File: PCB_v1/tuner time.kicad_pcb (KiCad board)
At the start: 4 copper layers, 80 x 40 mm, 109 parts, among them J1 B6B-PH-K-S, J10 1051640001, J2 B6B-PH-K-S, J3 S2B-PH-K-SLFSN, J4 Conn_01x05_Pin, J5 Conn_01x05_Pin, J6 Conn_02x04_Odd_Even, J7 B4B-XH-A, J8 Conn_ARM_JTAG_SWD_10, J9 Conn_01x03, SW1 SW_SPST, SW2 SW_Push, SW3 SW_Push, SW4 SW_Push, SW5 SW_Push, SW6 SW_Push, SW7 SW_Push, SW8 SW_Push, SW9 SW_SPDT, U1 C1F 2, U2 BQ25185DLHR, U3 BQ27441-G1, U4 DRV8834PWP, U5 STM32F405RGTx, U6 ESD9B5.0ST5G, Y1 ASE-8MHz-L-C-T

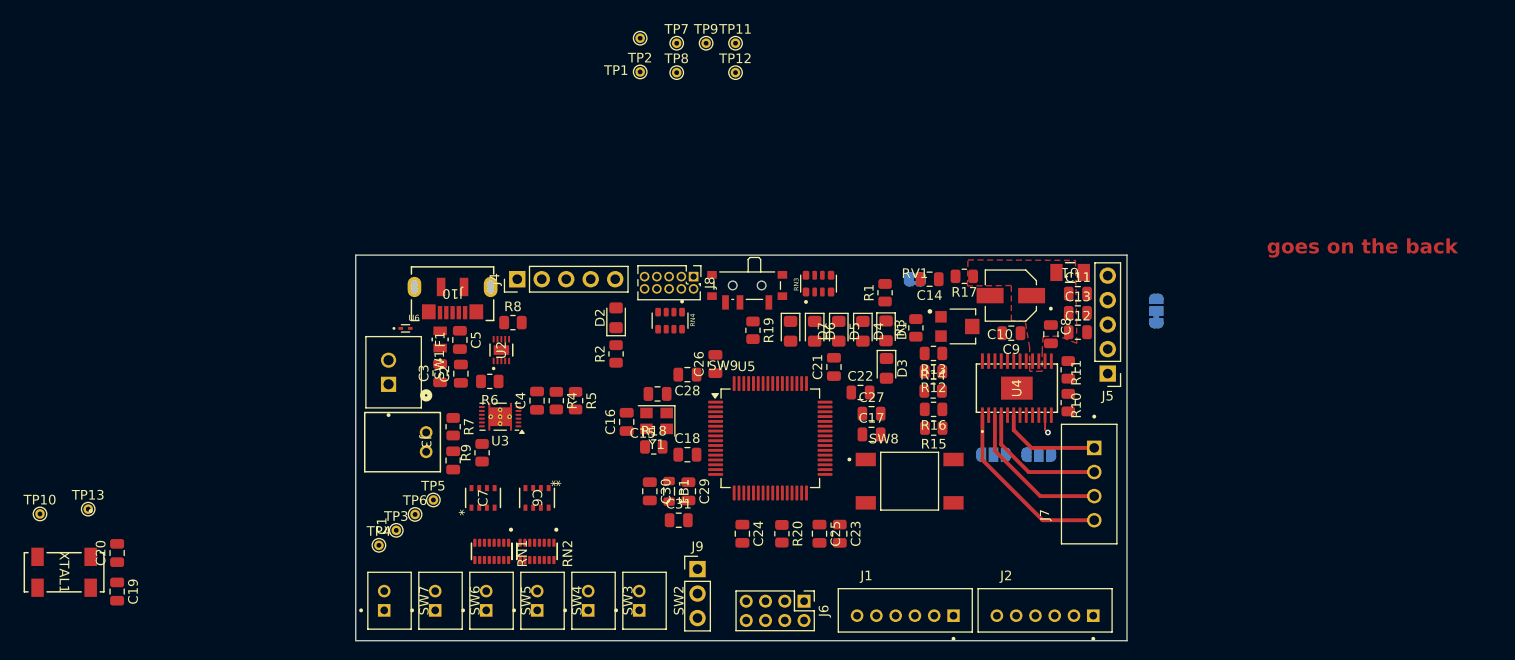
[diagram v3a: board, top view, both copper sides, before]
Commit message: Main routes done, no power planes, no DRC
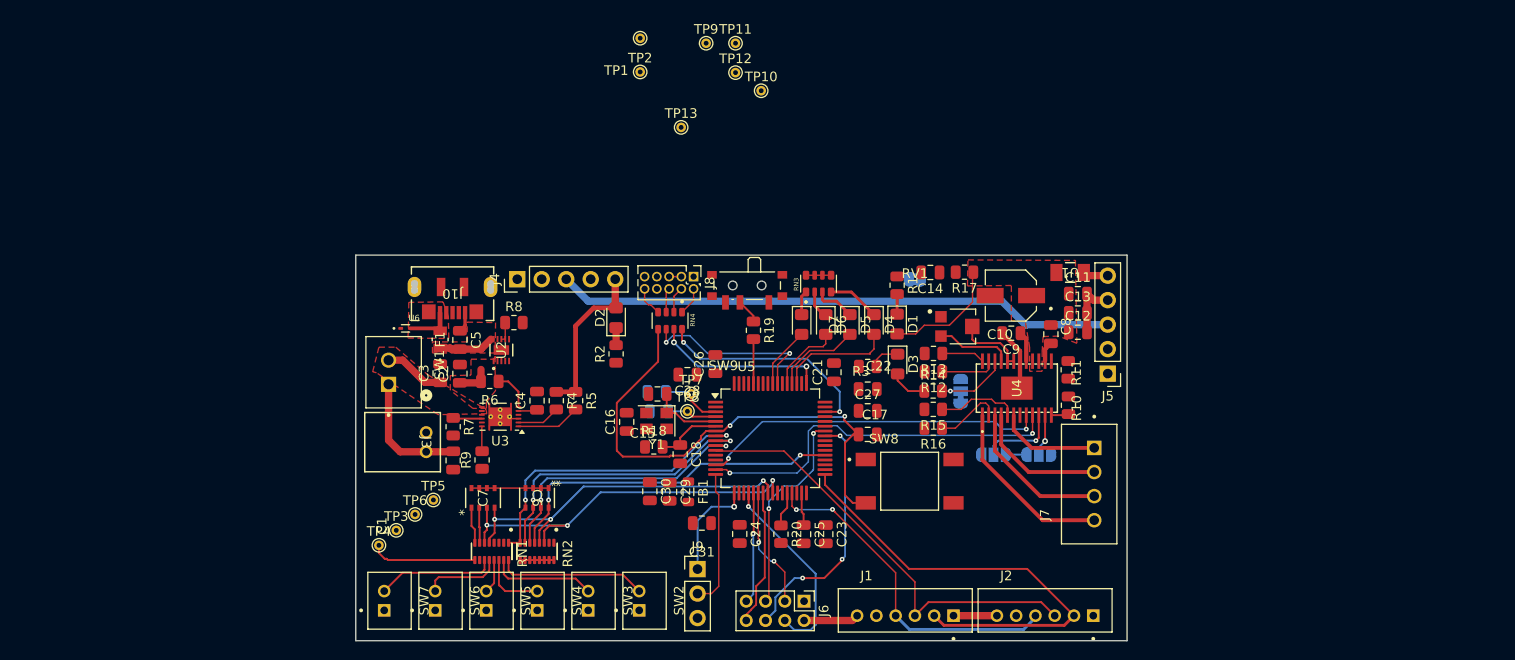
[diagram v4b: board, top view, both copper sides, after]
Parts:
- removed XTAL1: MC-306 32.7680K-E3:ROHS, Parts_Library:SO4_MC-306_SEC
- C19, C20: moved to B.Cu
- moved TP10 86.7 mm to (192.1, 83.0)
- moved TP13 73.2 mm to (183.8, 86.8)
- moved C19 59.7 mm to (181.2, 114.2), turned to 180 degrees
- moved C20 58.1 mm to (181.4, 116.2), turned to 180 degrees
- moved TP7 36.4 mm to (184.8, 114.4)
- moved TP8 35.1 mm to (184.4, 116.2)
- moved JP4 21.9 mm to (212.8, 114.1)
- moved R3 6.40 mm to (203.1, 111.5), turned to 180 degrees
- moved C31 2.42 mm to (185.9, 127.8), turned to 180 degrees
- moved FB1 2.00 mm to (184.5, 124.5)
- moved R15 1.95 mm to (209.9, 116.0)
- moved C29 1.95 mm to (182.6, 124.5)
- moved R16 1.95 mm to (209.9, 118.0)
- moved C25 1.65 mm to (196.4, 128.9)
- moved R1 1.47 mm to (206.2, 103.1), turned to -90 degrees
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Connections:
- D1 pad 2: 5V -> VMOT
- R3 pad 2: AGND -> GND
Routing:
- net VSYS: track 0.00 -> 61.7 mm
- net NRST: track 0.00 -> 52.5 mm, vias 0 -> 2
- net I2S_WS: track 0.00 -> 47.9 mm
- net I2S_DATA: track 0.00 -> 45.5 mm
- net Button6: track 0.00 -> 40.7 mm, vias 0 -> 3
- net DIR: track 0.00 -> 39.3 mm, vias 0 -> 2
- net Button5: track 0.00 -> 37.8 mm, vias 0 -> 3
- net Button4: track 0.00 -> 36.5 mm, vias 0 -> 2
- net STEP: track 0.00 -> 36.1 mm, vias 0 -> 2
- net 3V3: track 0.00 -> 35.8 mm
- net I2S_BCLK: track 0.00 -> 35.3 mm, vias 0 -> 2
- net Button1: track 0.00 -> 31.9 mm, vias 0 -> 2
- net Button2: track 0.00 -> 30.5 mm, vias 0 -> 2
- net Button3: track 0.00 -> 28.5 mm, vias 0 -> 2
- net DC: track 0.00 -> 26.2 mm, vias 0 -> 3
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- added copper zone on F.Cu, net BATT_POS
- added copper zone on F.Cu, net Net-(J10-VBUS)
- added copper zone on F.Cu, net VBUS
- added copper zone on F.Cu, net VSYS
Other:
- board text removed: "goes on the back"

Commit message: Power Layout done
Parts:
- added D8: Red, LED_SMD:LED_0805_2012Metric_Pad1.15x1.40mm_HandSolder, F.Cu at (172.1, 108.2)
- added D9: Red, LED_SMD:LED_0805_2012Metric_Pad1.15x1.40mm_HandSolder, F.Cu at (174.6, 108.1)
- added H1: MountingHole, MountingHole:MountingHole_2.2mm_M2_DIN965_Pad_TopOnly, F.Cu at (152.7, 102.7)
- added H2: MountingHole, MountingHole:MountingHole_2.2mm_M2_DIN965_Pad_TopOnly, F.Cu at (235.7, 139.8)
- added R21: 680, Resistor_SMD:R_0805_2012Metric, F.Cu at (172.1, 111.8)
- added R22: 1k, Resistor_SMD:R_0805_2012Metric, F.Cu at (174.6, 111.8)
- added R23: 10k, Resistor_SMD:R_0805_2012Metric, F.Cu at (164.5, 109.9)
- added U7: SMS05T1G, Parts_Library:SOIC_05T1G_ONS, F.Cu at (174.8, 130.6)
- added U8: SMS05T1G, Parts_Library:SOIC_05T1G_ONS, F.Cu at (159.8, 130.5)
- added XTAL1: MC-306 32.7680K-E3:ROHS, Parts_Library:SO4_MC-306_SEC, B.Cu at (168.3, 89.4)
- C2: value 10uF -> 22uF
- C3, C5: value 1uF -> 22uF
- J3: value S2B-PH-K-SLFSN -> JST_B2B-XH-A; footprint Parts_Library:CONN_S2B-PH-K-S_JST -> Parts_Library:JST_B2B-XH-A
- moved JP3 29.2 mm to (244.0, 129.5)
- moved JP2 19.3 mm to (238.8, 128.0)
- moved J3 11.0 mm to (153.7, 128.8)
- moved U2 10.2 mm to (155.0, 111.5)
- moved R6 9.53 mm to (154.6, 115.3), turned to 90 degrees
- moved R15 9.52 mm to (217.6, 121.6), turned to -90 degrees
- moved C1 9.47 mm to (163.8, 112.6), turned to -90 degrees
- moved C5 9.23 mm to (151.6, 109.8), turned to 90 degrees
- moved C2 9.21 mm to (151.6, 113.1)
- moved SW1 8.83 mm to (153.7, 121.0)
- moved R9 8.62 mm to (170.5, 116.8)
- moved TP3 7.65 mm to (160.7, 124.5)
- moved TP4 7.53 mm to (147.2, 135.6)
- moved R16 6.81 mm to (215.7, 121.6), turned to -90 degrees
- moved U6 4.81 mm to (159.9, 108.1), turned to 180 degrees
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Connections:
- net Net-(RN1A-R1.2) renamed /UI/B1
- net Net-(RN1B-R2.2) renamed /UI/B2
- net Net-(RN1C-R3.2) renamed /UI/B3
- net Net-(RN1D-R4.2) renamed /UI/B4
- net Net-(RN1E-R5.2) renamed /UI/B5
- net Net-(RN1F-R6.2) renamed /UI/B6
- net Net-(RN1G-R7.1) renamed /UI/B7
- net Net-(RN1H-R8.1) renamed /UI/B8
- C1 pad 2: Net-(SW1-A) -> BATT_POS
- C16 pad 1: +3.3V -> 3V3
- C21 pad 1: +3.3V -> 3V3
- C22 pad 1: +3.3V -> 3V3
- C23 pad 1: +3.3V -> 3V3
- C24 pad 1: +3.3V -> 3V3
- C26 pad 1: +3.3V -> 3V3
- C28 pad 1: +3.3V -> 3V3
- C3 pad 1: BATT_POS -> VBAT
- C31 pad 1: +3.3V -> 3V3
- FB1 pad 2: +3.3V -> 3V3
- J8 pad 1: +3.3V -> 3V3
- R6 pad 2: VSYS -> VBAT
- R9 pad 2: Net-(U3-GPOUT) -> BAT_EMPTY
- SW9 pad 1: +3V3 -> 3V3
- U2 pad 2: BATT_POS -> VBAT
- U2 pad 3: unconnected-(U2-STAT2-Pad3) -> STATS2
- U2 pad 6: GND -> Net-(U2-TS/MR)
- U2 pad 9: unconnected-(U2-STAT1-Pad9) -> STATS1
- U3 pad 12: Net-(U3-GPOUT) -> BAT_EMPTY
- U3 pad 7: VSYS -> VBAT
- U5 pad 1: +3.3V -> 3V3
- U5 pad 19: +3.3V -> 3V3
- U5 pad 32: +3.3V -> 3V3
- U5 pad 43: unconnected-(U5-PA10-Pad43) -> BAT_EMPTY
- U5 pad 48: +3.3V -> 3V3
- U5 pad 64: +3.3V -> 3V3
- Y1 pad 4: +3.3V -> 3V3
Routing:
- net DIR: track 39.3 -> 0.00 mm, vias 2 -> 0
- net NRST: track 52.5 -> 27.7 mm, vias 2 -> 3
- net Button6: track 40.7 -> 19.8 mm, vias 3 -> 1
- net BATT_POS: track 10.4 -> 28.1 mm
- net Button2: track 30.5 -> 13.0 mm
- net Button1: track 31.9 -> 14.6 mm
- net Button4: track 36.5 -> 19.5 mm
- net Button3: track 28.5 -> 11.5 mm
- net Button5: track 37.8 -> 20.8 mm, vias 3 -> 1
- net /Motor/A1: track 18.8 -> 2.10 mm
- net 3V3: track 35.8 -> 19.9 mm
- net /Motor/A2: track 15.9 -> 1.76 mm
- net Net-(SW1-A): track 13.0 -> 0.00 mm
- net Net-(RN1H-R8.2): track 11.1 -> 0.00 mm
- net /Motor/B1: track 10.7 -> 0.00 mm
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- added copper zone on F.Cu, net GND
- added copper zone on F.Cu, net VBAT

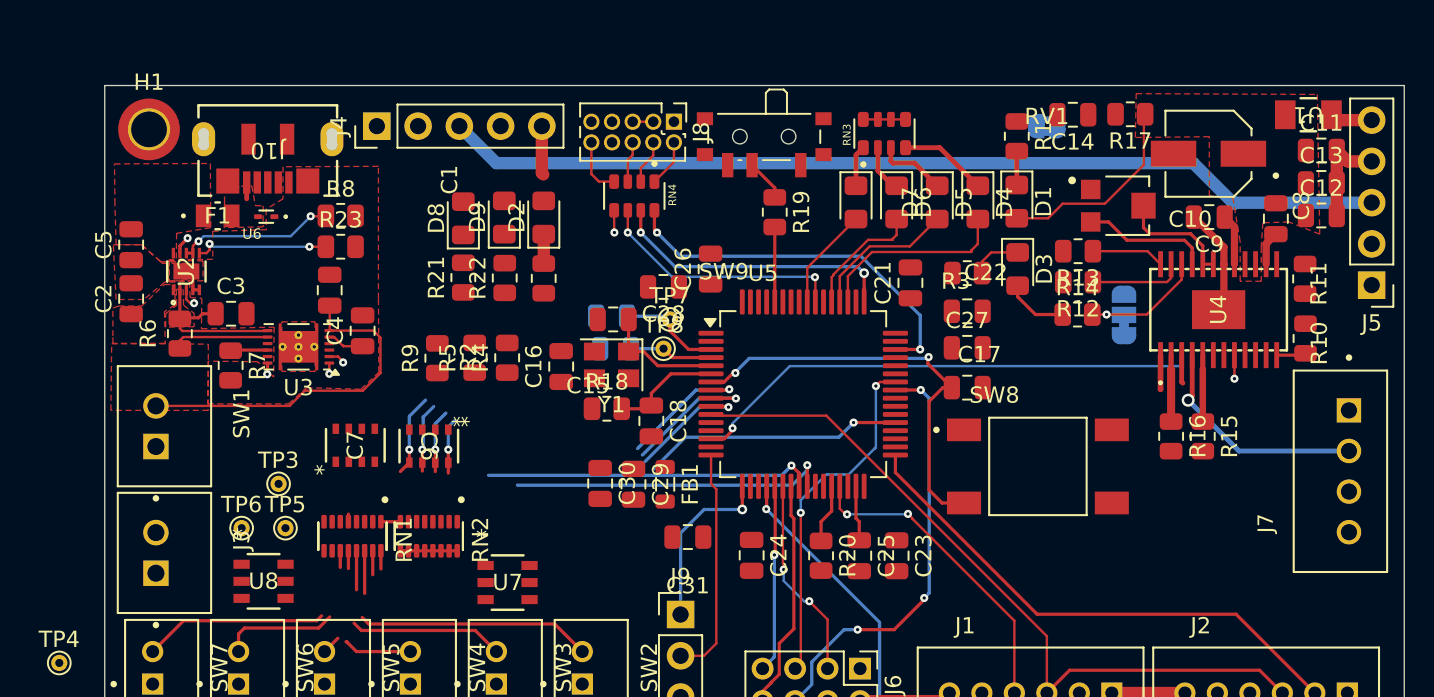
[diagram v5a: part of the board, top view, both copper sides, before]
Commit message: adding the libraries and the new bom for footprint
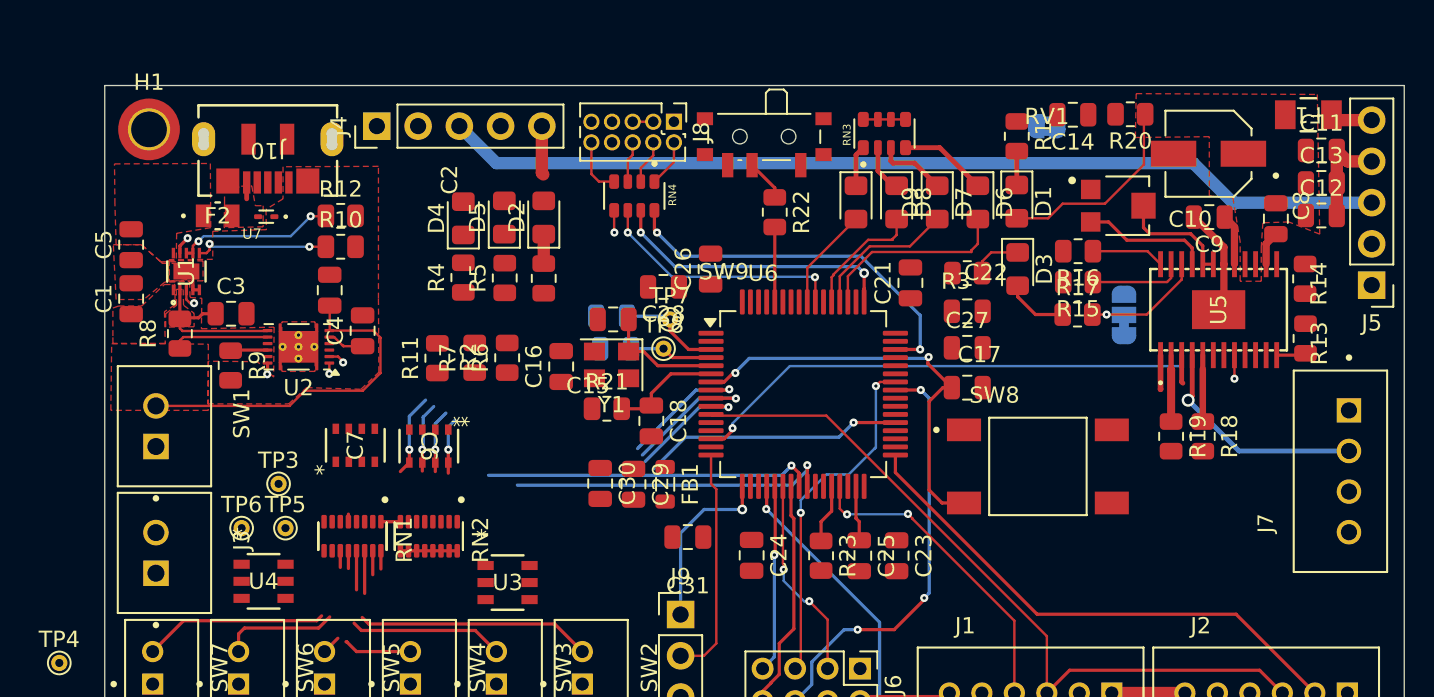
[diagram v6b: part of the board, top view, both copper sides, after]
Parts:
- renumbered C2 to C1, C1 to C2, D8 to D4, D9 to D5, D4 to D6, D5 to D7, D6 to D8, D7 to D9, U1 to F1, F1 to F2, R23 to R10, R9 to R11, R8 to R12, R10 to R13, R11 to R14, R12 to R15, R13 to R16, R14 to R17, R15 to R18, R16 to R19, R17 to R20, R18 to R21, R19 to R22, R20 to R23, R21 to R4, R22 to R5, R4 to R6, R5 to R7, R6 to R8, R7 to R9, U2 to U1, U3 to U2, U7 to U3, U8 to U4, U4 to U5, U5 to U6, U6 to U7

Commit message: adding the crystal
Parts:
- C10: footprint Parts_Library:CAP_EEE1AA101WR -> Library:CAP_EEE1AA101WR
- C30, C31: footprint Capacitor_SMD:C_0805_2012Metric -> Capacitor_SMD:C_1206_3216Metric_Pad1.33x1.80mm_HandSolder
- F1: footprint Parts_Library:C1_BEL -> Library:C1_BEL
- F2: footprint Parts_Library:FUS_VISHAY_MFU0805_VIS -> Library:FUS_VISHAY_MFU0805_VIS
- FB1: footprint Inductor_SMD:L_0805_2012Metric -> Inductor_SMD:L_0603_1608Metric
- J10: footprint Parts_Library:CON00906_5_MOL -> Library:CON00906_5_MOL
- J3: footprint Parts_Library:JST_B2B-XH-A -> Library:JST_B2B-XH-A
- J6: value Conn_02x04_Odd_Even -> OLED Conn_02x04; footprint Connector_PinHeader_2.00mm:PinHeader_2x04_P2.00mm_Vertical -> Connector_PinHeader_2.54mm:PinHeader_2x04_P2.54mm_Vertical
- J8: footprint Connector_PinHeader_1.27mm:PinHeader_2x05_P1.27mm_Vertical -> Connector_PinHeader_2.54mm:PinHeader_2x05_P2.54mm_Vertical
- RN3: value 660 -> 680
- SW1: footprint Parts_Library:JST_B2B-XH-A -> GT_library:JST_B2B-PH-K-S
- SW8: footprint Parts_Library:SW_TS04-66-65-BK-160-SMT -> Library:SW_TS04-66-65-BK-160-SMT
- U1: footprint Parts_Library:WSON10_DLH_TEX -> Library:WSON10_DLH_TEX
- U3, U4: footprint Parts_Library:SOIC_05T1G_ONS -> Library:SOIC_05T1G_ONS
- U5: footprint Parts_Library:SOP65P640X120-25N -> Library:SOP65P640X120-25N
- Y1: value ASE-8MHz-L-C-T -> Crystal; footprint Oscillator:Oscillator_SMD_Abracon_ASE-4Pin_3.2x2.5mm -> Library:LFXTAL003237Bulk
- moved Y1 32.6 mm to (194.6, 87.5), turned to 0 degrees
- moved C30 32.3 mm to (188.6, 93.2), turned to 0 degrees
- moved C31 31.4 mm to (188.6, 96.5), turned to 0 degrees
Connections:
- R21 pad 1: Net-(Y1-OUT) -> unconnected-(R21-Pad1)
- Y1 pad 1: PH0-OSCIN -> unconnected-(Y1-Pad1)
- Y1 pad 2: GND -> unconnected-(Y1-Pad2)

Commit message: before oscilator
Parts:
- C1, C11, C12, C13, C14, C15, C16, C17, C18, C19, C2, C20, C21, C22, C23, C24, C25, C26, C27, C28, C29, C3, C4, C5, C8, C9: footprint Capacitor_SMD:C_0805_2012Metric -> C_0805_2012Metric
- C10: footprint Library:CAP_EEE1AA101WR -> CAP_EEE1AA101WR
- C30, C31: footprint Capacitor_SMD:C_1206_3216Metric_Pad1.33x1.80mm_HandSolder -> C_1206_3216Metric_Pad1.33x1.80mm_HandSolder
- C6, C7: footprint GT_library:CAP_CA0612_3P2X1P6_YAG -> CAP_CA0612_3P2X1P6_YAG
- D1, D2, D3, D4, D5, D6, D7, D8, D9: footprint LED_SMD:LED_0805_2012Metric_Pad1.15x1.40mm_HandSolder -> LED_0805_2012Metric_Pad1.15x1.40mm_HandSolder
- F1: footprint Library:C1_BEL -> C1_BEL
- F2: footprint Library:FUS_VISHAY_MFU0805_VIS -> FUS_VISHAY_MFU0805_VIS
- FB1: footprint Inductor_SMD:L_0603_1608Metric -> L_0603_1608Metric
- H1, H2: footprint MountingHole:MountingHole_2.2mm_M2_DIN965_Pad_TopOnly -> MountingHole_2.2mm_M2_DIN965_Pad_TopOnly
- J1, J2: footprint GT_library:JST_B6B-PH-K-S -> JST_B6B-PH-K-S
- J10: footprint Library:CON00906_5_MOL -> CON00906_5_MOL
- J3: footprint Library:JST_B2B-XH-A -> JST_B2B-XH-A
- J4, J5: footprint Connector_PinHeader_2.54mm:PinHeader_1x05_P2.54mm_Vertical -> PinHeader_1x05_P2.54mm_Vertical
- J6: footprint Connector_PinHeader_2.54mm:PinHeader_2x04_P2.54mm_Vertical -> PinHeader_2x04_P2.54mm_Vertical
- J7: footprint Parts_Library:JST_B4B-XH-A -> JST_B4B-XH-A
- J8: footprint Connector_PinHeader_2.54mm:PinHeader_2x05_P2.54mm_Vertical -> PinHeader_2x05_P2.54mm_Vertical
- J9: footprint Connector_PinHeader_2.54mm:PinHeader_1x03_P2.54mm_Vertical -> PinHeader_1x03_P2.54mm_Vertical
- JP1: footprint Jumper:SolderJumper-2_P1.3mm_Bridged2Bar_RoundedPad1.0x1.5mm -> SolderJumper-2_P1.3mm_Bridged2Bar_RoundedPad1.0x1.5mm
- JP2, JP3: footprint Jumper:SolderJumper-3_P1.3mm_Open_RoundedPad1.0x1.5mm -> SolderJumper-3_P1.3mm_Open_RoundedPad1.0x1.5mm
- JP4: footprint Jumper:SolderJumper-3_P1.3mm_Bridged12_RoundedPad1.0x1.5mm -> SolderJumper-3_P1.3mm_Bridged12_RoundedPad1.0x1.5mm
- R1, R10, R11, R12, R13, R14, R15, R16, R17, R18, R19, R2, R20, R21, R22, R23, R3, R4, R5, R6, R7, R8, R9: footprint Resistor_SMD:R_0805_2012Metric -> R_0805_2012Metric
- RN1, RN2: footprint Parts_Library:RESCAXE50P280X160X55-16N -> RESCAXE50P280X160X55-16N
- RN3: footprint Parts_Library:RESCAXS80P320X160X60-8N -> RESCAXS80P320X160X60-8N
- RN4: footprint Parts_Library:RESCAXE80P320X160X70-8N -> RESCAXE80P320X160X70-8N
- RV1: footprint Parts_Library:TRIM_TC33X-2-103E -> TRIM_TC33X-2-103E
- SW1, SW2, SW3, SW4, SW5, SW6, SW7: footprint GT_library:JST_B2B-PH-K-S -> JST_B2B-PH-K-S
- SW8: footprint Library:SW_TS04-66-65-BK-160-SMT -> SW_TS04-66-65-BK-160-SMT
- SW9: footprint Button_Switch_SMD:SW_SPDT_PCM12 -> SW_SPDT_PCM12
- TP1, TP10, TP11, TP12, TP13, TP2, TP3, TP4, TP5, TP6, TP7, TP8, TP9: footprint TestPoint:TestPoint_THTPad_D1.0mm_Drill0.5mm -> TestPoint_THTPad_D1.0mm_Drill0.5mm
- U1: footprint Library:WSON10_DLH_TEX -> WSON10_DLH_TEX
- U2: footprint Package_SON:Texas_S-PDSO-N12 -> Texas_S-PDSO-N12
- U3, U4: footprint Library:SOIC_05T1G_ONS -> SOIC_05T1G_ONS
- U5: footprint Library:SOP65P640X120-25N -> SOP65P640X120-25N
- U6: footprint Package_QFP:LQFP-64_10x10mm_P0.5mm -> LQFP-64_10x10mm_P0.5mm
- U7: footprint Parts_Library:SODFL1006X40N -> SODFL1006X40N
- XTAL1: footprint Parts_Library:SO4_MC-306_SEC -> SO4_MC-306_SEC
- Y1: footprint Library:LFXTAL003237Bulk -> LFXTAL003237Bulk
- moved Y1 5.34 mm to (199.8, 88.9), turned to 90 degrees
